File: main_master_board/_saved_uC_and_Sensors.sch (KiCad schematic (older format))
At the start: 41 parts, among them P14 CONN_01X05, U1 NRF24L01+, U15 DSPIC33EP512GP806-I/PT, U16 DWM1000, U29 RGB_LED, U30 RGB_LED, U31 Si1900DL, U32 Si1900DL, U9 Si1900DL

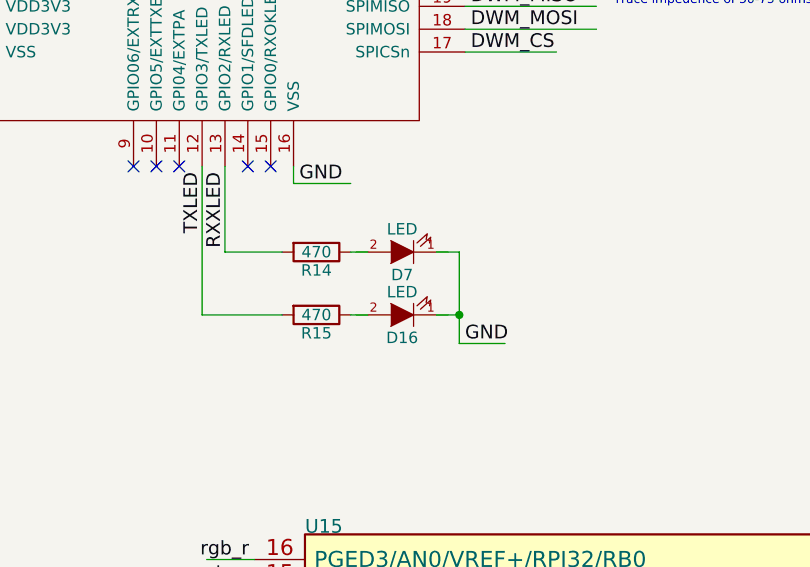
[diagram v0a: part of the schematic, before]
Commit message: Placed all compnenets on board. Now need to route!
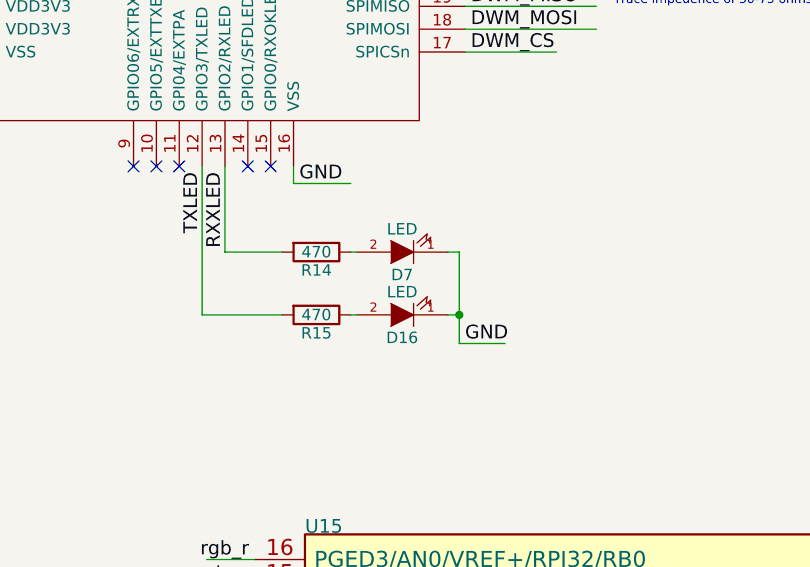
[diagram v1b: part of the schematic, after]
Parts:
- C16, C17, C18, C20, C21, C22, C23, C24, C31: footprint Capacitors_SMD:C_0603 -> Capacitors_SMD:C_0402
- R35, R54, R55, R56, R57, R58, R63: footprint Resistors_SMD:R_0603 -> Resistors_SMD:R_0402
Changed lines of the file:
@@
 F 0 "C21" V 11110 8045 50  0000 L CNN
 F 1 "100nF" V 11120 7725 50  0000 L CNN
-F 2 "Capacitors_SMD:C_0603" H 11060 7995 50  0001 C CNN
+F 2 "Capacitors_SMD:C_0402" H 11060 7995 50  0001 C CNN
 F 3 "" H 11060 7995 50  0000 C CNN
 	1    11060 7995
@@
 F 0 "C22" V 11110 8195 50  0000 L CNN
 F 1 "100nF" V 11120 7875 50  0000 L CNN
-F 2 "Capacitors_SMD:C_0603" H 11060 8145 50  0001 C CNN
+F 2 "Capacitors_SMD:C_0402" H 11060 8145 50  0001 C CNN
 F 3 "" H 11060 8145 50  0000 C CNN
 	1    11060 8145
@@
 F 0 "C23" V 11110 8345 50  0000 L CNN
 F 1 "100nF" V 11120 8025 50  0000 L CNN
-F 2 "Capacitors_SMD:C_0603" H 11060 8295 50  0001 C CNN
+F 2 "Capacitors_SMD:C_0402" H 11060 8295 50  0001 C CNN
 F 3 "" H 11060 8295 50  0000 C CNN
 	1    11060 8295
@@
 F 0 "C24" V 11110 8495 50  0000 L CNN
 F 1 "100nF" V 11120 8175 50  0000 L CNN
-F 2 "Capacitors_SMD:C_0603" H 11060 8445 50  0001 C CNN
+F 2 "Capacitors_SMD:C_0402" H 11060 8445 50  0001 C CNN
 F 3 "" H 11060 8445 50  0000 C CNN
 	1    11060 8445
@@
 F 0 "C31" V 11110 8645 50  0000 L CNN
 F 1 "100nF" V 11120 8325 50  0000 L CNN
-F 2 "Capacitors_SMD:C_0603" H 11060 8595 50  0001 C CNN
+F 2 "Capacitors_SMD:C_0402" H 11060 8595 50  0001 C CNN
 F 3 "" H 11060 8595 50  0000 C CNN
 	1    11060 8595
@@
 F 0 "C20" H 8610 4470 50  0000 L CNN
 F 1 "100nF" V 8500 4275 50  0000 L CNN
-F 2 "Capacitors_SMD:C_0603" H 8600 4400 50  0001 C CNN
+F 2 "Capacitors_SMD:C_0402" H 8600 4400 50  0001 C CNN
 F 3 "" H 8600 4400 50  0000 C CNN
 	1    8600 4400
@@
 F 0 "C18" H 8460 4345 50  0000 L CNN
 F 1 "100nF" V 8350 4150 50  0000 L CNN
-F 2 "Capacitors_SMD:C_0603" H 8450 4275 50  0001 C CNN
+F 2 "Capacitors_SMD:C_0402" H 8450 4275 50  0001 C CNN
 F 3 "" H 8450 4275 50  0000 C CNN
 	1    8450 4275
@@
 F 0 "C17" H 8310 4220 50  0000 L CNN
 F 1 "100nF" V 8200 4025 50  0000 L CNN
-F 2 "Capacitors_SMD:C_0603" H 8300 4150 50  0001 C CNN
+F 2 "Capacitors_SMD:C_0402" H 8300 4150 50  0001 C CNN
 F 3 "" H 8300 4150 50  0000 C CNN
 	1    8300 4150
@@
 F 0 "C16" H 8160 4095 50  0000 L CNN
 F 1 "100nF" V 8050 3900 50  0000 L CNN
-F 2 "Capacitors_SMD:C_0603" H 8150 4025 50  0001 C CNN
+F 2 "Capacitors_SMD:C_0402" H 8150 4025 50  0001 C CNN
 F 3 "" H 8150 4025 50  0000 C CNN
 	1    8150 4025
@@
 F 0 "R56" V 4775 3550 50  0000 C CNN
 F 1 "43.2" V 4725 3400 50  0000 C CNN
-F 2 "Resistors_SMD:R_0603" V 4655 3400 50  0001 C CNN
+F 2 "Resistors_SMD:R_0402" V 4655 3400 50  0001 C CNN
 F 3 "" H 4725 3400 50  0000 C CNN
 	1    4725 3400
@@
 F 0 "R57" V 4775 3650 50  0000 C CNN
 F 1 "4" V 4725 3500 50  0000 C CNN
-F 2 "Resistors_SMD:R_0603" V 4655 3500 50  0001 C CNN
+F 2 "Resistors_SMD:R_0402" V 4655 3500 50  0001 C CNN
 F 3 "" H 4725 3500 50  0000 C CNN
 	1    4725 3500
@@
 F 0 "R58" V 4775 3750 50  0000 C CNN
 F 1 "4" V 4725 3600 50  0000 C CNN
-F 2 "Resistors_SMD:R_0603" V 4655 3600 50  0001 C CNN
+F 2 "Resistors_SMD:R_0402" V 4655 3600 50  0001 C CNN
 F 3 "" H 4725 3600 50  0000 C CNN
 	1    4725 3600
@@
 F 0 "R35" V 4750 4250 50  0000 C CNN
 F 1 "43.2" V 4700 4100 50  0000 C CNN
-F 2 "Resistors_SMD:R_0603" V 4630 4100 50  0001 C CNN
+F 2 "Resistors_SMD:R_0402" V 4630 4100 50  0001 C CNN
 F 3 "" H 4700 4100 50  0000 C CNN
 	1    4700 4100
@@
 F 0 "R54" V 4750 4350 50  0000 C CNN
 F 1 "4" V 4700 4200 50  0000 C CNN
-F 2 "Resistors_SMD:R_0603" V 4630 4200 50  0001 C CNN
+F 2 "Resistors_SMD:R_0402" V 4630 4200 50  0001 C CNN
 F 3 "" H 4700 4200 50  0000 C CNN
 	1    4700 4200
@@
 F 0 "R55" V 4750 4450 50  0000 C CNN
 F 1 "4" V 4700 4300 50  0000 C CNN
-F 2 "Resistors_SMD:R_0603" V 4630 4300 50  0001 C CNN
+F 2 "Resistors_SMD:R_0402" V 4630 4300 50  0001 C CNN
 F 3 "" H 4700 4300 50  0000 C CNN
 	1    4700 4300
@@
 F 0 "R63" V 4625 4875 50  0000 C CNN
 F 1 "10" V 4575 4725 50  0000 C CNN
-F 2 "Resistors_SMD:R_0603" V 4505 4725 50  0001 C CNN
+F 2 "Resistors_SMD:R_0402" V 4505 4725 50  0001 C CNN
 F 3 "" H 4575 4725 50  0000 C CNN
 	1    4575 4725
@@
 	9000 1975 9000 2350
 Wire Wire Line
-	9550 2625 9625 2625
-Wire Wire Line
-	9550 2350 9625 2350
-Wire Wire Line
-	9925 2350 10025 2350
-Wire Wire Line
 	10025 2350 10025 2750
 Wire Wire Line
 	10025 2750 10225 2750
-Wire Wire Line
-	9925 2625 10025 2625
 Connection ~ 10025 2625
 Wire Wire Line
@@
 Wire Wire Line
 	4725 4725 5150 4725
+Wire Wire Line
+	9550 2350 9575 2350
+Wire Wire Line
+	9550 2625 9575 2625
+Wire Wire Line
+	9975 2350 10025 2350
+Wire Wire Line
+	9975 2625 10025 2625
 $EndSCHEMATC
